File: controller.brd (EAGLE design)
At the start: 56.8 x 64.8 mm, 30 parts, among them IC1 MEGA8-P, IC2 VREG-LM340, IC3 MAX6675, J1 ICSP, Q1 16.0Mhz

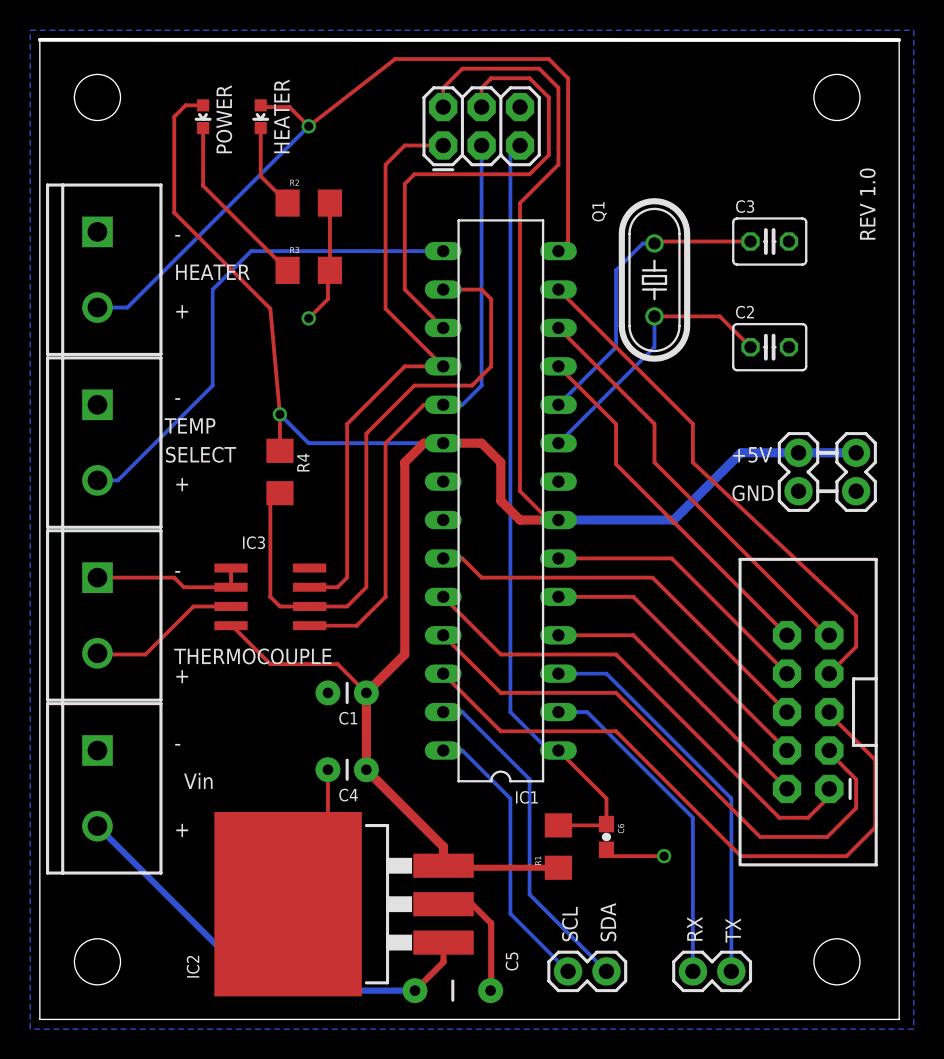
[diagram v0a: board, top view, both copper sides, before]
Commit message: Fixed orientation of screw terminals.
Screw terminals were oriented with receptacle facing inwards towards
the center of the board. Rotated them and performed some pin swaps.

Also added silk to label contrast trim pot on interface board.
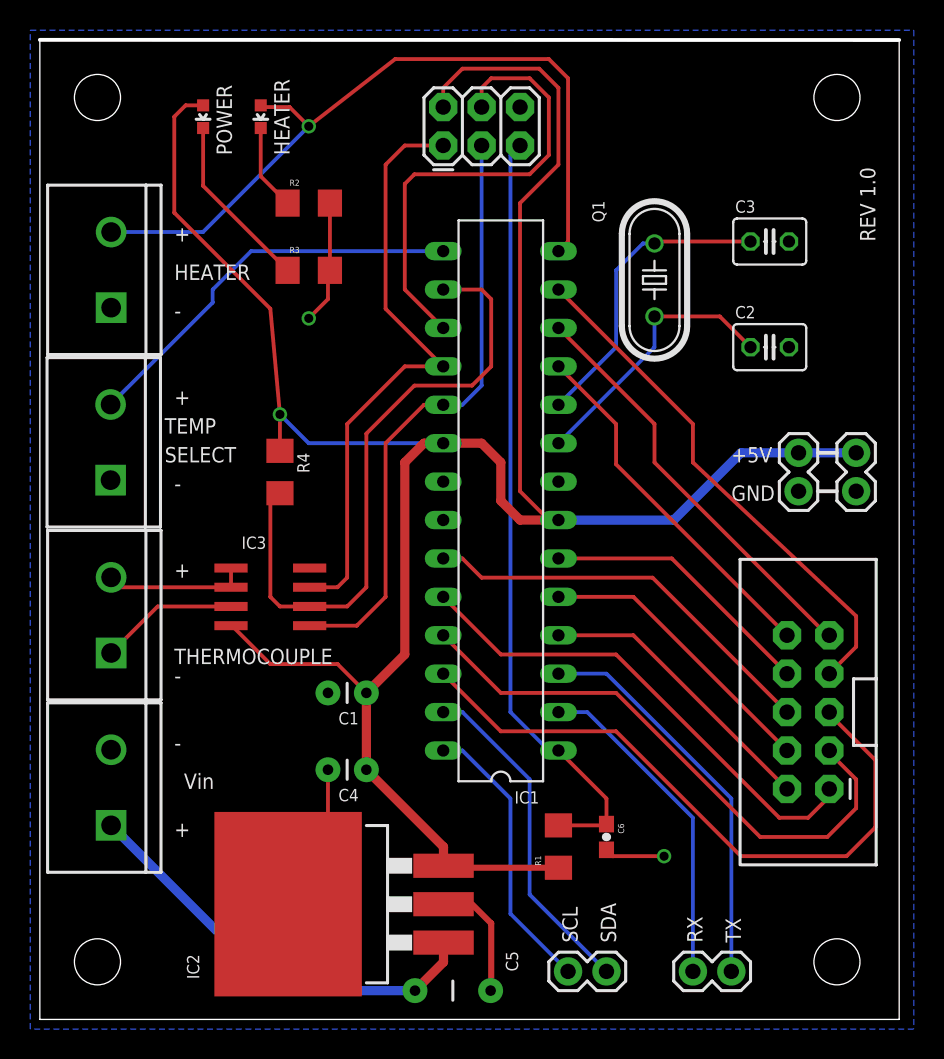
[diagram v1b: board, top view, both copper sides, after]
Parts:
- moved JP2 5.09 mm to (4.71, 47.1), turned to 90 degrees
- moved JP1 5.06 mm to (4.71, 24.2), turned to 90 degrees
- moved JP4 5.06 mm to (4.68, 35.7), turned to 90 degrees
- moved JP5 5.03 mm to (4.71, 12.8), turned to 90 degrees
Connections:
- net 9VIN: now also JP5.1; no longer JP5.2
- net GND: now also JP1.2, JP5.2; no longer JP1.1, JP5.1
- net TC+: now also JP1.1; no longer JP1.2
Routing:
- net SW_1: track 32.9 -> 26.7 mm
- net HTR_OUT: track 53.6 -> 50.6 mm
- net TC+: track 10.2 -> 9.20 mm
- net GND: track 43.2 -> 42.3 mm
- net 9VIN: track 29.5 -> 28.6 mm
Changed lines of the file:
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@@
 <setting verticaltext="up"/>
 </settings>
-<grid distance="0.025" unitdist="inch" unit="inch" style="dots" multiple="1" display="yes" altdistance="0.0125" altunitdist="inch" altunit="inch"/>
+<grid distance="0.025" unitdist="inch" unit="inch" style="dots" multiple="1" display="yes" altdistance="0" altunitdist="inch" altunit="inch"/>
 <layers>
 <layer number="1" name="Top" color="4" fill="1" visible="yes" active="yes"/>
@@
 <text x="8.255" y="36.83" size="1.016" layer="121" ratio="12">SELECT</text>
 <text x="9.525" y="15.24" size="1.016" layer="121" ratio="12">Vin</text>
-<text x="8.89" y="46.355" size="1.016" layer="121" ratio="12">+</text>
-<text x="8.89" y="34.925" size="1.016" layer="121" ratio="12">+</text>
-<text x="8.89" y="22.225" size="1.016" layer="121" ratio="12">+</text>
+<text x="8.89" y="51.435" size="1.016" layer="121" ratio="12">+</text>
+<text x="8.89" y="40.64" size="1.016" layer="121" ratio="12">+</text>
+<text x="8.89" y="29.21" size="1.016" layer="121" ratio="12">+</text>
 <text x="8.89" y="12.065" size="1.016" layer="121" ratio="12">+</text>
 <text x="8.89" y="17.78" size="1.016" layer="121" ratio="12">-</text>
-<text x="8.89" y="29.21" size="1.016" layer="121" ratio="12">-</text>
-<text x="8.89" y="40.64" size="1.016" layer="121" ratio="12">-</text>
-<text x="8.89" y="51.435" size="1.016" layer="121" ratio="12">-</text>
+<text x="8.89" y="22.225" size="1.016" layer="121" ratio="12">-</text>
+<text x="8.89" y="34.925" size="1.016" layer="121" ratio="12">-</text>
+<text x="8.89" y="46.355" size="1.016" layer="121" ratio="12">-</text>
 <text x="8.89" y="23.495" size="1.016" layer="121" ratio="12">THERMOCOUPLE</text>
 <text x="38.1" y="5.08" size="1.016" layer="121" ratio="12" rot="R90">SDA</text>
@@
 <attribute name="NAME" x="21.082" y="20.32" size="0.8128" layer="25" rot="R180"/>
 </element>
-<element name="JP1" library="SparkFun-Connectors" package="SCREWTERMINAL-5MM-2" value="Thermocouple" x="3.81" y="29.21" smashed="yes" rot="R270"/>
-<element name="JP2" library="SparkFun-Connectors" package="SCREWTERMINAL-5MM-2" value="Heater" x="3.81" y="52.07" smashed="yes" rot="R270"/>
+<element name="JP1" library="SparkFun-Connectors" package="SCREWTERMINAL-5MM-2" value="Thermocouple" x="4.712746875" y="24.229309375" smashed="yes" rot="R90"/>
+<element name="JP2" library="SparkFun-Connectors" package="SCREWTERMINAL-5MM-2" value="Heater" x="4.7147" y="47.062378125" smashed="yes" rot="R90"/>
 <element name="JP3" library="SparkFun-Connectors" package="2X5-SHROUDED_LOCK" value="M05X2SHD_LOCK" x="50.8" y="20.32" smashed="yes" rot="R180">
 <attribute name="NAME" x="53.721" y="31.242" size="0.4064" layer="104" rot="R180"/>
@@
 <attribute name="VALUE" x="24.765" y="58.42" size="1.016" layer="27" ratio="12" rot="R90"/>
 </element>
-<element name="JP4" library="SparkFun-Connectors" package="SCREWTERMINAL-5MM-2" value="Switch" x="3.81" y="40.64" smashed="yes" rot="R270"/>
+<element name="JP4" library="SparkFun-Connectors" package="SCREWTERMINAL-5MM-2" value="Switch" x="4.676296875" y="35.658125" smashed="yes" rot="R90"/>
 <element name="IC3" library="SparkFun-AnalogIC" package="SO08-MAX6675" value="MAX6675" x="15.24" y="27.94" smashed="yes" rot="R270">
 <attribute name="NAME" x="13.335" y="31.115" size="0.8128" layer="25"/>
@@
 <attribute name="NAME" x="17.018" y="37.465" size="0.8128" layer="25" rot="R270"/>
 </element>
-<element name="JP5" library="SparkFun-Connectors" package="SCREWTERMINAL-5MM-2" value="Vin" x="3.81" y="17.78" smashed="yes" rot="R270"/>
+<element name="JP5" library="SparkFun-Connectors" package="SCREWTERMINAL-5MM-2" value="Vin" x="4.71115" y="12.833065625" smashed="yes" rot="R90"/>
 <element name="R1" library="SparkFun-Resistors" package="1206" value="10kOhm" x="34.29" y="11.43" smashed="yes" rot="R90">
 <attribute name="NAME" x="33.147" y="10.16" size="0.4064" layer="25" rot="R90"/>
@@
 <contactref element="IC1" pad="8"/>
 <contactref element="C1" pad="2"/>
-<contactref element="JP1" pad="1"/>
+<contactref element="JP1" pad="2"/>
 <contactref element="J1" pad="6"/>
 <contactref element="JP2" pad="1"/>
@@
 <contactref element="R3" pad="2"/>
 <contactref element="R2" pad="2"/>
-<contactref element="JP5" pad="1"/>
+<contactref element="JP5" pad="2"/>
 <contactref element="C4" pad="2"/>
 <contactref element="C5" pad="2"/>
@@
 <via x="17.78" y="46.355" extent="1-16" drill="0.6"/>
 <via x="41.275" y="10.795" extent="1-16" drill="0.6"/>
-<wire x1="12.64" y1="28.575" x2="9.525" y2="28.575" width="0.254" layer="1"/>
-<wire x1="9.525" y1="28.575" x2="8.89" y2="29.21" width="0.254" layer="1"/>
-<wire x1="8.89" y1="29.21" x2="3.81" y2="29.21" width="0.254" layer="1"/>
 <wire x1="12.64" y1="28.575" x2="12.64" y2="29.845" width="0.254" layer="1"/>
 <wire x1="19.18" y1="53.975" x2="19.18" y2="49.53" width="0.254" layer="1"/>
@@
 <wire x1="37.885" y1="10.795" x2="37.465" y2="11.215" width="0.254" layer="1"/>
 <contactref element="JP9" pad="1"/>
+<wire x1="12.64" y1="28.575" x2="5.36705625" y2="28.575" width="0.254" layer="1"/>
+<wire x1="5.36705625" y1="28.575" x2="4.712746875" y2="29.229309375" width="0.254" layer="1"/>
 </signal>
 <signal name="ICSP_RESET">
@@
 <contactref element="JP2" pad="2"/>
 <contactref element="LED2" pad="A"/>
-<wire x1="3.81" y1="47.07" x2="5.795" y2="47.07" width="0.254" layer="16"/>
-<wire x1="5.795" y1="47.07" x2="17.78" y2="59.055" width="0.254" layer="16"/>
 <via x="17.78" y="59.055" extent="1-16" drill="0.6"/>
 <wire x1="17.78" y1="59.055" x2="16.51" y2="60.325" width="0.254" layer="1"/>
@@
 <wire x1="34.925" y1="62.23" x2="34.925" y2="51.435" width="0.254" layer="1"/>
 <wire x1="34.925" y1="51.435" x2="34.29" y2="50.8" width="0.254" layer="1"/>
+<wire x1="4.7147" y1="52.062378125" x2="10.787378125" y2="52.062378125" width="0.254" layer="16"/>
+<wire x1="10.787378125" y1="52.062378125" x2="17.78" y2="59.055" width="0.254" layer="16"/>
 </signal>
 <signal name="TC+">
-<contactref element="JP1" pad="2"/>
+<contactref element="JP1" pad="1"/>
 <contactref element="IC3" pad="3"/>
-<wire x1="3.81" y1="24.21" x2="3.89" y2="24.13" width="0.254" layer="1"/>
-<wire x1="3.89" y1="24.13" x2="6.985" y2="24.13" width="0.254" layer="1"/>
-<wire x1="6.985" y1="24.13" x2="10.16" y2="27.305" width="0.254" layer="1"/>
-<wire x1="10.16" y1="27.305" x2="12.64" y2="27.305" width="0.254" layer="1"/>
+<wire x1="12.64" y1="27.305" x2="7.7884375" y2="27.305" width="0.254" layer="1"/>
+<wire x1="7.7884375" y1="27.305" x2="4.712746875" y2="24.229309375" width="0.254" layer="1"/>
 </signal>
 <signal name="BTN1">
@@
 <contactref element="JP4" pad="2"/>
 <contactref element="IC1" pad="15"/>
-<wire x1="3.81" y1="35.64" x2="5.16" y2="35.64" width="0.254" layer="16"/>
-<wire x1="5.16" y1="35.64" x2="11.43" y2="41.91" width="0.254" layer="16"/>
-<wire x1="11.43" y1="41.91" x2="11.43" y2="48.26" width="0.254" layer="16"/>
 <wire x1="11.43" y1="48.26" x2="13.97" y2="50.8" width="0.254" layer="16"/>
 <wire x1="13.97" y1="50.8" x2="26.67" y2="50.8" width="0.254" layer="16"/>
+<wire x1="11.43" y1="48.26" x2="11.43" y2="47.402284375" width="0.254" layer="16"/>
+<wire x1="11.43" y1="47.402284375" x2="4.676296875" y2="40.658125" width="0.254" layer="16"/>
 </signal>
 <signal name="N$1">
@@
 </signal>
 <signal name="9VIN" class="1">
-<contactref element="JP5" pad="2"/>
+<contactref element="JP5" pad="1"/>
 <contactref element="C5" pad="1"/>
 <contactref element="IC2" pad="1"/>
-<wire x1="24.805" y1="1.905" x2="26.69" y2="3.79" width="0.4064" layer="1"/>
-<wire x1="26.69" y1="3.79" x2="26.69" y2="5.08" width="0.4064" layer="1"/>
-<wire x1="3.81" y1="12.78" x2="14.685" y2="1.905" width="0.4064" layer="16"/>
-<wire x1="14.685" y1="1.905" x2="24.805" y2="1.905" width="0.4064" layer="16"/>
+<wire x1="24.805" y1="1.905" x2="26.69" y2="3.79" width="0.6096" layer="1"/>
+<wire x1="26.69" y1="3.79" x2="26.69" y2="5.08" width="0.6096" layer="1"/>
+<wire x1="24.805" y1="1.905" x2="15.639215625" y2="1.905" width="0.6096" layer="16"/>
+<wire x1="15.639215625" y1="1.905" x2="4.71115" y2="12.833065625" width="0.6096" layer="16"/>
 </signal>
 <signal name="XTAL2">

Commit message: Changed 1 of the aux power connectors to molex polarized header.
Made change for interface and for controller boards
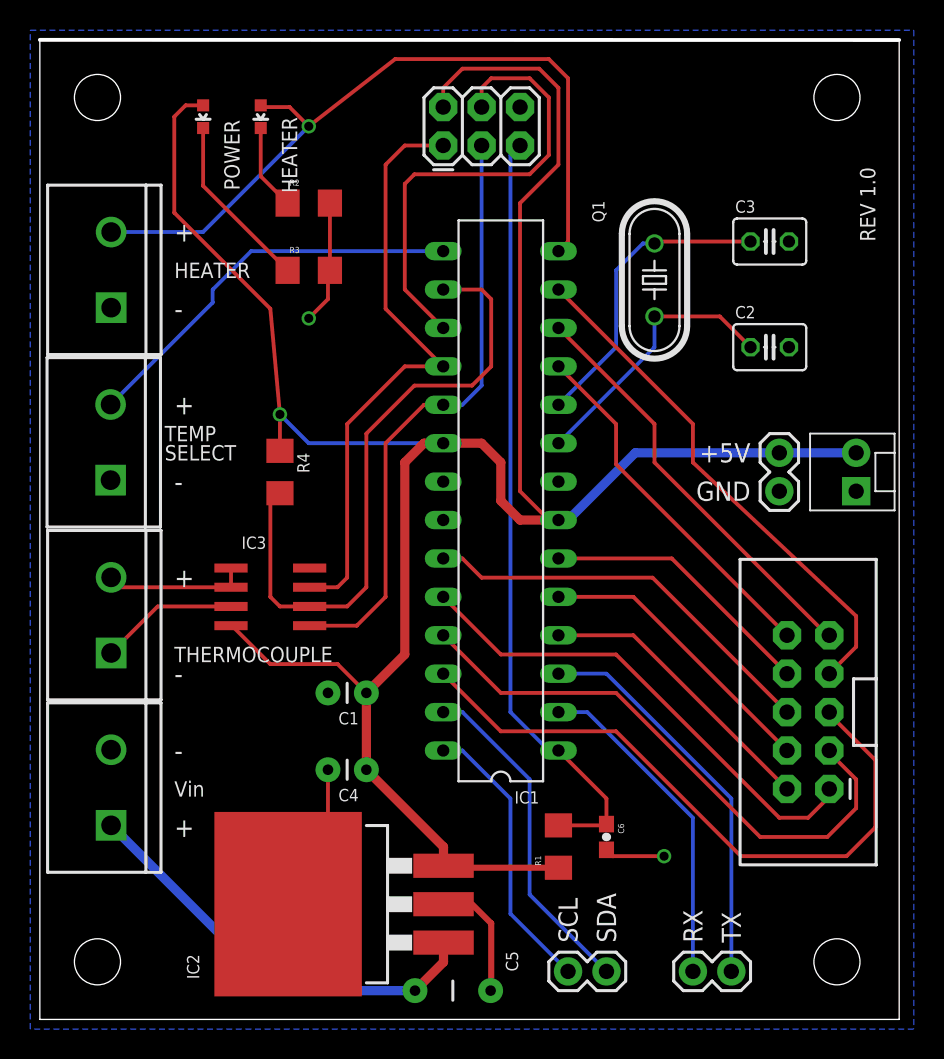
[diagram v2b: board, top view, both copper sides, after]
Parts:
- JP9: device SparkFun-Connectors:1X02 -> SparkFun-Connectors:MOLEX-1X2
- moved JP8 1.27 mm to (48.9, 34.9)
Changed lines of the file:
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@@
 <wire x1="56.82" y1="64.76" x2="0" y2="64.77" width="0.254" layer="20"/>
 <wire x1="0" y1="64.77" x2="0" y2="0" width="0" layer="20"/>
-<text x="8.89" y="48.895" size="1.016" layer="121" ratio="12">HEATER</text>
-<text x="8.255" y="38.735" size="1.016" layer="121" ratio="12">TEMP</text>
-<text x="8.255" y="36.83" size="1.016" layer="121" ratio="12">SELECT</text>
-<text x="9.525" y="15.24" size="1.016" layer="121" ratio="12">Vin</text>
-<text x="8.89" y="51.435" size="1.016" layer="121" ratio="12">+</text>
-<text x="8.89" y="40.64" size="1.016" layer="121" ratio="12">+</text>
-<text x="8.89" y="29.21" size="1.016" layer="121" ratio="12">+</text>
-<text x="8.89" y="12.065" size="1.016" layer="121" ratio="12">+</text>
-<text x="8.89" y="17.78" size="1.016" layer="121" ratio="12">-</text>
-<text x="8.89" y="22.225" size="1.016" layer="121" ratio="12">-</text>
-<text x="8.89" y="34.925" size="1.016" layer="121" ratio="12">-</text>
-<text x="8.89" y="46.355" size="1.016" layer="121" ratio="12">-</text>
-<text x="8.89" y="23.495" size="1.016" layer="121" ratio="12">THERMOCOUPLE</text>
-<text x="38.1" y="5.08" size="1.016" layer="121" ratio="12" rot="R90">SDA</text>
-<text x="35.56" y="5.08" size="1.016" layer="121" ratio="12" rot="R90">SCL</text>
-<text x="46.355" y="5.08" size="1.016" layer="121" ratio="12" rot="R90">TX</text>
-<text x="43.815" y="5.08" size="1.016" layer="121" ratio="12" rot="R90">RX</text>
-<text x="45.72" y="36.83" size="1.016" layer="121" ratio="12">+5V</text>
-<text x="45.72" y="34.29" size="1.016" layer="121" ratio="12">GND</text>
-<wire x1="51.435" y1="37.465" x2="52.705" y2="37.465" width="0.254" layer="121"/>
-<wire x1="51.435" y1="34.925" x2="52.705" y2="34.925" width="0.254" layer="121"/>
-<text x="16.51" y="57.15" size="1.016" layer="121" ratio="12" rot="R90">HEATER</text>
-<text x="12.7" y="57.15" size="1.016" layer="121" ratio="12" rot="R90">POWER</text>
+<text x="8.89" y="49.53" size="1.016" layer="121" ratio="12" align="center-left">HEATER</text>
+<text x="8.255" y="38.735" size="1.016" layer="121" ratio="12" align="center-left">TEMP</text>
+<text x="8.255" y="37.465" size="1.016" layer="121" ratio="12" align="center-left">SELECT</text>
+<text x="8.89" y="15.24" size="1.016" layer="121" ratio="12" align="center-left">Vin</text>
+<text x="8.89" y="52.07" size="1.27" layer="121" ratio="12" align="center-left">+</text>
+<text x="8.89" y="40.64" size="1.27" layer="121" ratio="12" align="center-left">+</text>
+<text x="8.89" y="29.21" size="1.27" layer="121" ratio="12" align="center-left">+</text>
+<text x="8.89" y="12.7" size="1.27" layer="121" ratio="12" align="center-left">+</text>
+<text x="8.89" y="17.78" size="1.27" layer="121" ratio="12" align="center-left">-</text>
+<text x="8.89" y="22.86" size="1.27" layer="121" ratio="12" align="center-left">-</text>
+<text x="8.89" y="35.56" size="1.27" layer="121" ratio="12" align="center-left">-</text>
+<text x="8.89" y="46.99" size="1.27" layer="121" ratio="12" align="center-left">-</text>
+<text x="8.89" y="24.13" size="1.016" layer="121" ratio="12" align="center-left">THERMOCOUPLE</text>
+<text x="37.465" y="5.08" size="1.27" layer="121" ratio="12" rot="R90" align="center-left">SDA</text>
+<text x="34.925" y="5.08" size="1.27" layer="121" ratio="12" rot="R90" align="center-left">SCL</text>
+<text x="45.72" y="5.08" size="1.27" layer="121" ratio="12" rot="R90" align="center-left">TX</text>
+<text x="43.18" y="5.08" size="1.27" layer="121" ratio="12" rot="R90" align="center-left">RX</text>
+<text x="46.99" y="37.465" size="1.27" layer="121" ratio="12" align="center-right">+5V</text>
+<text x="46.99" y="34.925" size="1.27" layer="121" ratio="12" align="center-right">GND</text>
+<text x="16.51" y="57.15" size="1.016" layer="121" ratio="12" rot="R90" align="center">HEATER</text>
+<text x="12.7" y="57.15" size="1.016" layer="121" ratio="12" rot="R90" align="center">POWER</text>
 <text x="55.245" y="51.435" size="1.016" layer="121" ratio="12" rot="R90">REV 1.0</text>
 </plain>
@@
 </element>
 <element name="J1" library="SparkFun-Connectors" package="2X3" value="ICSP" x="26.67" y="57.785" smashed="yes">
-<attribute name="VALUE" x="24.765" y="58.42" size="1.016" layer="27" ratio="12" rot="R90"/>
+<attribute name="VALUE" x="24.765" y="58.42" size="1.016" layer="27" ratio="12" rot="R90" align="center"/>
 </element>
 <element name="JP4" library="SparkFun-Connectors" package="SCREWTERMINAL-5MM-2" value="Switch" x="4.676296875" y="35.658125" smashed="yes" rot="R90"/>
@@
 </element>
 <element name="JP7" library="SparkFun-Connectors" package="1X02" value="I2C" x="34.925" y="3.175" smashed="yes"/>
-<element name="JP8" library="SparkFun-Connectors" package="1X02" value="PWR_AUX" x="50.165" y="34.925" smashed="yes" rot="R90"/>
+<element name="JP8" library="SparkFun-Connectors" package="1X02" value="PWR_AUX" x="48.895" y="34.925" smashed="yes" rot="R90"/>
 <element name="U$2" library="SparkFun-Electromechanical" package="STAND-OFF-TIGHT" value="" x="3.81" y="60.96"/>
 <element name="U$3" library="SparkFun-Electromechanical" package="STAND-OFF-TIGHT" value="" x="3.81" y="3.81"/>
 <element name="U$4" library="SparkFun-Electromechanical" package="STAND-OFF-TIGHT" value="" x="52.705" y="60.96"/>
 <element name="U$5" library="SparkFun-Electromechanical" package="STAND-OFF-TIGHT" value="" x="52.705" y="3.81" rot="R90"/>
-<element name="JP9" library="SparkFun-Connectors" package="1X02" value="PWR_AUX" x="53.975" y="34.925" smashed="yes" rot="R90"/>
+<element name="JP9" library="SparkFun-Connectors" package="MOLEX-1X2" value="PWR_AUX" x="53.975" y="34.925" smashed="yes" rot="R90"/>
 </elements>
 <signals>
@@
 <wire x1="31.75" y1="53.975" x2="31.75" y2="34.925" width="0.254" layer="1"/>
 <wire x1="31.75" y1="34.925" x2="33.655" y2="33.02" width="0.254" layer="1"/>
-<wire x1="34.29" y1="33.02" x2="41.91" y2="33.02" width="0.6096" layer="16"/>
-<wire x1="41.91" y1="33.02" x2="46.355" y2="37.465" width="0.6096" layer="16"/>
-<wire x1="46.355" y1="37.465" x2="50.165" y2="37.465" width="0.6096" layer="16"/>
 <contactref element="JP9" pad="2"/>
-<wire x1="50.165" y1="37.465" x2="53.975" y2="37.465" width="0.6096" layer="16"/>
 <wire x1="34.29" y1="10.03" x2="26.82" y2="10.03" width="0.4064" layer="1"/>
 <wire x1="26.82" y1="10.03" x2="26.69" y2="10.16" width="0.4064" layer="1"/>
 <wire x1="26.69" y1="10.16" x2="26.69" y2="11.41" width="0.6096" layer="1"/>
 <wire x1="26.69" y1="11.41" x2="21.59" y2="16.51" width="0.6096" layer="1"/>
+<wire x1="34.29" y1="33.02" x2="34.925" y2="33.02" width="0.6096" layer="16"/>
+<wire x1="34.925" y1="33.02" x2="39.37" y2="37.465" width="0.6096" layer="16"/>
+<wire x1="39.37" y1="37.465" x2="48.895" y2="37.465" width="0.6096" layer="16"/>
+<wire x1="48.895" y1="37.465" x2="53.975" y2="37.465" width="0.6096" layer="16"/>
 </signal>
 <signal name="MAX_MISO">
